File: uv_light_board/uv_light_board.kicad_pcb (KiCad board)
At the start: 2 copper layers, 14 parts, among them J1 Power, J2 Power

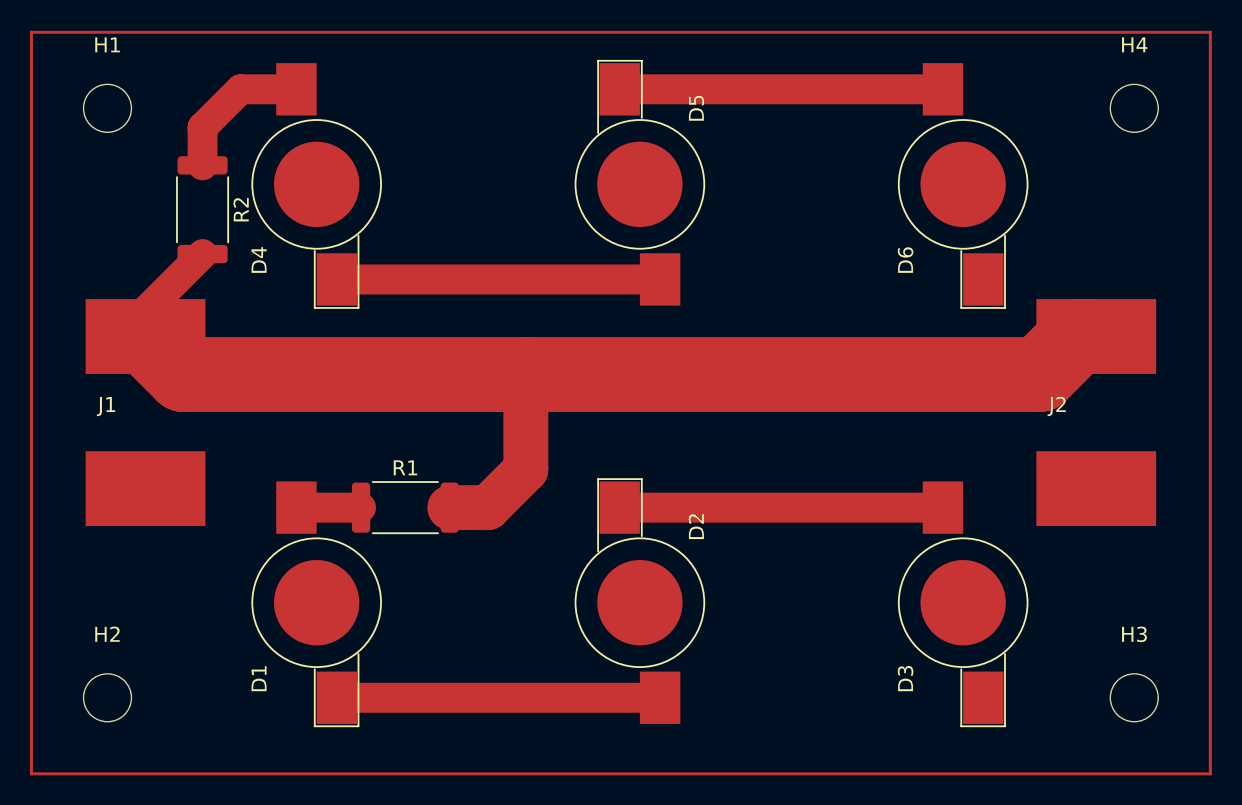
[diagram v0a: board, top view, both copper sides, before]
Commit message: Updating control board to include more pinouts
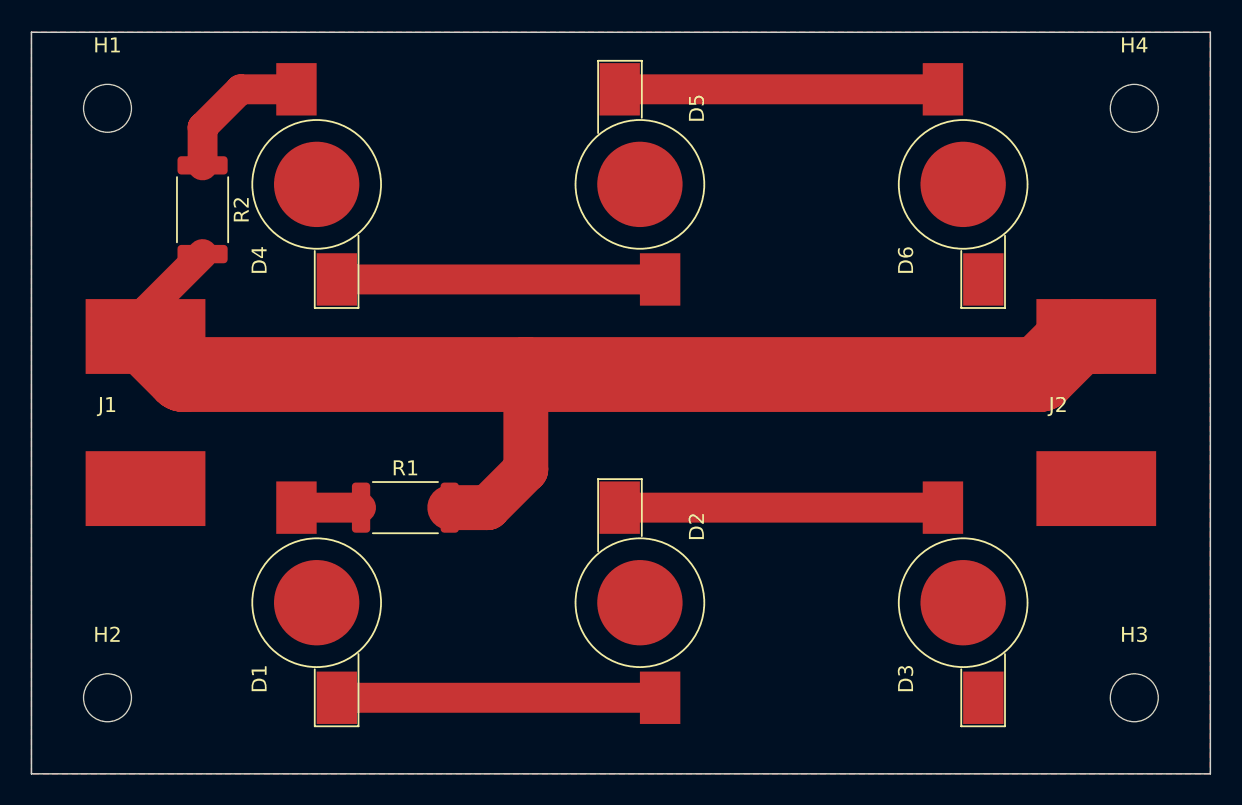
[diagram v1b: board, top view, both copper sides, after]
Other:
- board outline added: 78.7 x 49.5 mm
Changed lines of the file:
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@@
       (outputformat 1)
       (mirror false)
-      (drillshape 1)
+      (drillshape 0)
       (scaleselection 1)
-      (outputdirectory "")
+      (outputdirectory "export/")
     )
   )
@@
     (fp_line (start 3.15 -1.6) (end 3.15 1.6) (layer "F.Fab") (width 0.1))
     (fp_line (start -3.15 1.6) (end -3.15 -1.6) (layer "F.Fab") (width 0.1))
-    (pad "1" smd roundrect (at -2.9625 0 270) (size 1.225 3.35) (layers "F.Cu" "F.Paste" "F.Mask") (roundrect_rratio 0.204082)
+    (pad "1" smd roundrect (at -2.9625 0 270) (size 1.225 3.35) (layers "F.Cu" "F.Paste" "F.Mask") (roundrect_rratio 0.2040816327)
       (net 9 "Net-(D4-Pad2)") (pintype "passive"))
-    (pad "2" smd roundrect (at 2.9625 0 270) (size 1.225 3.35) (layers "F.Cu" "F.Paste" "F.Mask") (roundrect_rratio 0.204082)
+    (pad "2" smd roundrect (at 2.9625 0 270) (size 1.225 3.35) (layers "F.Cu" "F.Paste" "F.Mask") (roundrect_rratio 0.2040816327)
       (net 14 "+12V") (pintype "passive"))
     (model "${KICAD6_3DMODEL_DIR}/Resistor_SMD.3dshapes/R_2512_6332Metric.wrl"
@@
     (fp_line (start 3.15 -1.6) (end 3.15 1.6) (layer "F.Fab") (width 0.1))
     (fp_line (start -3.15 -1.6) (end 3.15 -1.6) (layer "F.Fab") (width 0.1))
-    (pad "1" smd roundrect (at -2.9625 0) (size 1.225 3.35) (layers "F.Cu" "F.Paste" "F.Mask") (roundrect_rratio 0.204082)
+    (pad "1" smd roundrect (at -2.9625 0) (size 1.225 3.35) (layers "F.Cu" "F.Paste" "F.Mask") (roundrect_rratio 0.2040816327)
       (net 2 "Net-(D1-Pad2)") (pintype "passive"))
-    (pad "2" smd roundrect (at 2.9625 0) (size 1.225 3.35) (layers "F.Cu" "F.Paste" "F.Mask") (roundrect_rratio 0.204082)
+    (pad "2" smd roundrect (at 2.9625 0) (size 1.225 3.35) (layers "F.Cu" "F.Paste" "F.Mask") (roundrect_rratio 0.2040816327)
       (net 14 "+12V") (pintype "passive"))
     (model "${KICAD6_3DMODEL_DIR}/Resistor_SMD.3dshapes/R_2512_6332Metric.wrl"
@@
     (pad "" np_thru_hole circle (at 0 0) (size 3.2 3.2) (drill 3.2) (layers *.Cu *.Mask))
   )
-  (gr_rect (start 143.51 71.12) (end 222.25 120.65) (layer "F.Cu") (width 0.2) (fill none))
+  (gr_rect (start 143.51 71.12) (end 222.25 120.65) (layer "Edge.Cuts") (width 0.1) (fill none))
   (segment (start 185.5 115.57) (end 163.91 115.57) (width 2) (layer "F.Cu") (net 1))
   (segment (start 165.525 102.87) (end 161.21 102.87) (width 2) (layer "F.Cu") (net 2))
